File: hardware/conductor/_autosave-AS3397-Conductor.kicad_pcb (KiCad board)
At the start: 2 copper layers, 97.3 x 97.8 mm, 49 parts, among them J1 Micro_SD_Card, J10 Conn_FX_2, J11 I2C controller, J12 Conn_01x03_Socket_AudioOUT, J13 Voice connector, J14 Conn_01x02_Socket, J15 I2C controller, J16 Conn_01x06_Socket_SPI, J17 Conn_01x03_Socket, J18 Conn_01x03_Socket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

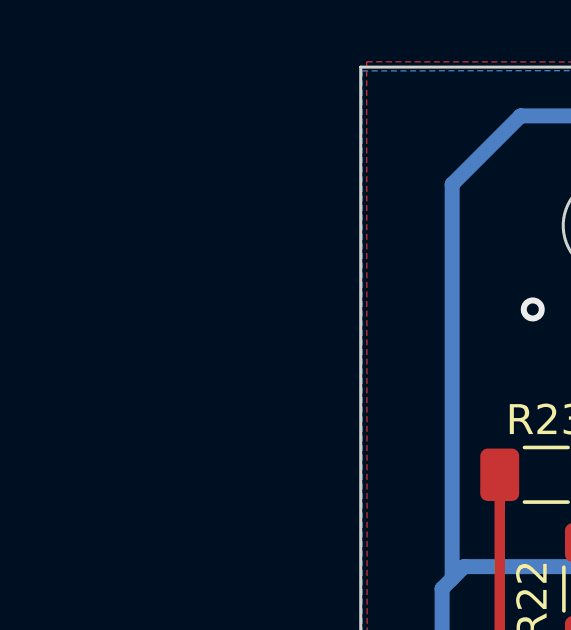
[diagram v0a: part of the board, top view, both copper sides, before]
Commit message: Conductor Board : Fixing MIDI routing
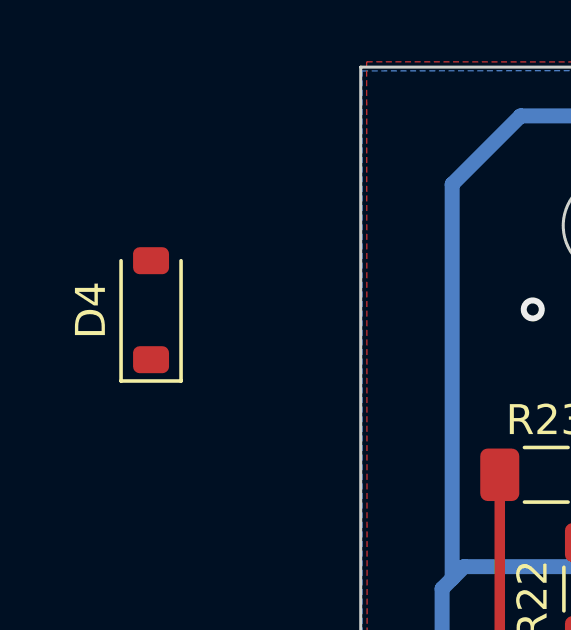
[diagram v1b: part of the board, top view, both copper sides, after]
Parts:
- added D4: 1N4148W, Diode_SMD:D_SOD-123, F.Cu at (98.2, 66.2)
